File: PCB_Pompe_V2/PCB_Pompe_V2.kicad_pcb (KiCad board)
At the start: 4 copper layers, 89.8 x 59.2 mm, 197 parts, among them J1 Conn_01x04_Female, J10 Conn_01x03_Female, J11 Conn_01x03_Female, J12 Conn_01x03_Female, J13 Conn_01x05_Female, J14 Conn_01x03_Female, J15 Conn_01x03_Female, J16 Conn_01x03_Female, J17 Conn_01x03_Female, J18 Conn_01x03_Female, J19 Conn_01x03_Female, J2 Conn_01x04_Female, J3 Conn_01x03_Female, J4 Conn_01x03_Female, J5 Conn_01x03_Female, J6 Conn_01x03_Female, J7 Conn_01x03_Female, J8 Conn_01x02_Male, J9 Conn_01x03_Female, Q1 DMN10H700S, Q10 DMN10H700S, Q11 DMN10H700S, Q12 DMN10H700S, Q13 DMN10H700S, Q14 DMN10H700S, Q15 DMN10H700S, Q16 DMN10H700S, Q17 DMN10H700S, Q18 DMN10H700S, Q19 DMN10H700S, Q2 DMN10H700S, Q20 DMN10H700S, Q21 DMN10H700S, Q22 DMN10H700S, Q23 DMN10H700S, Q24 DMN10H700S, Q25 DMN10H700S, Q26 DMN10H700S, Q27 DMN10H700S, Q28 DMN10H700S, Q29 DMN10H700S, Q3 DMN10H700S, Q30 DMN10H700S, Q4 DMN10H700S, Q5 DMN10H700S, Q6 DMN10H700S, Q7 DMN10H700S, Q8 DMN10H700S, Q9 DMN10H700S, U1 SN65HVD232, U2 STM32F302C6Tx, U3 NCP1117-3.3_SOT223, Y1 8MHz

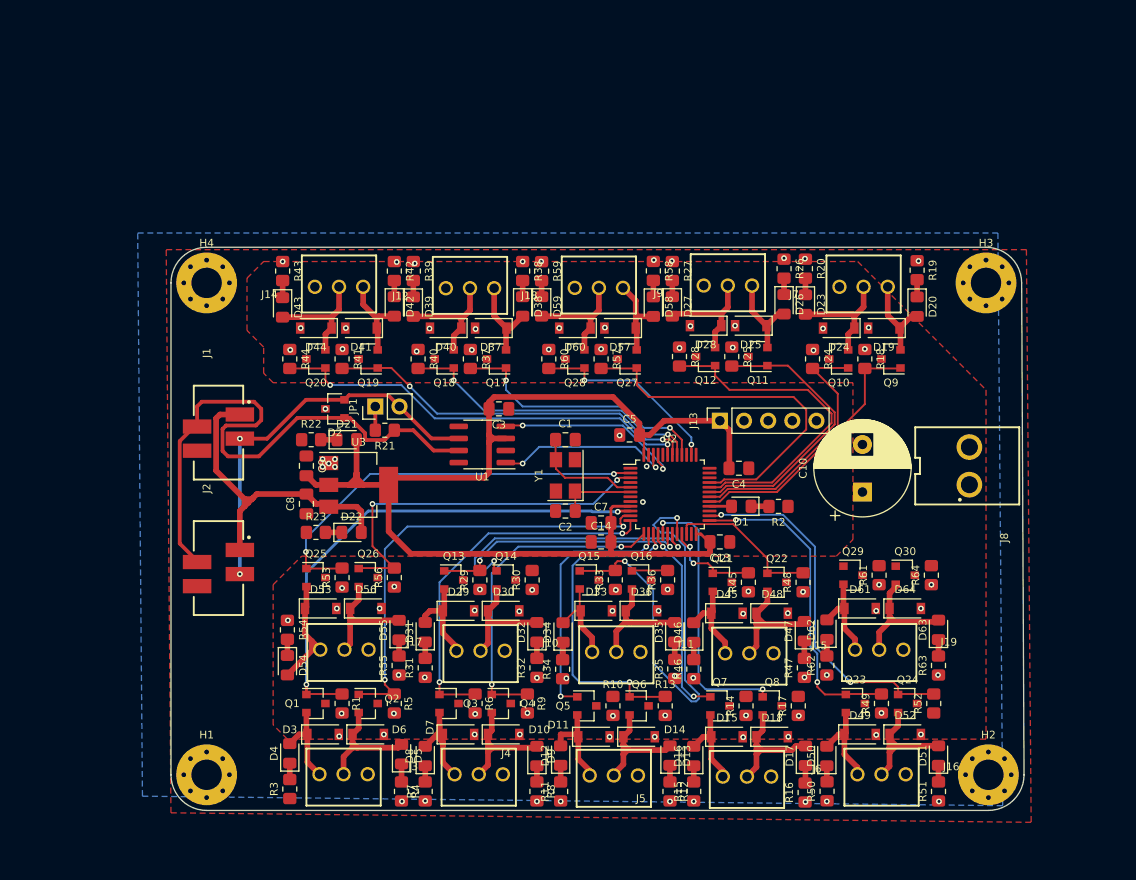
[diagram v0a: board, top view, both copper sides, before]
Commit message: IO prete, Pompe finir sérigraphie, Alim+AX12 à faire
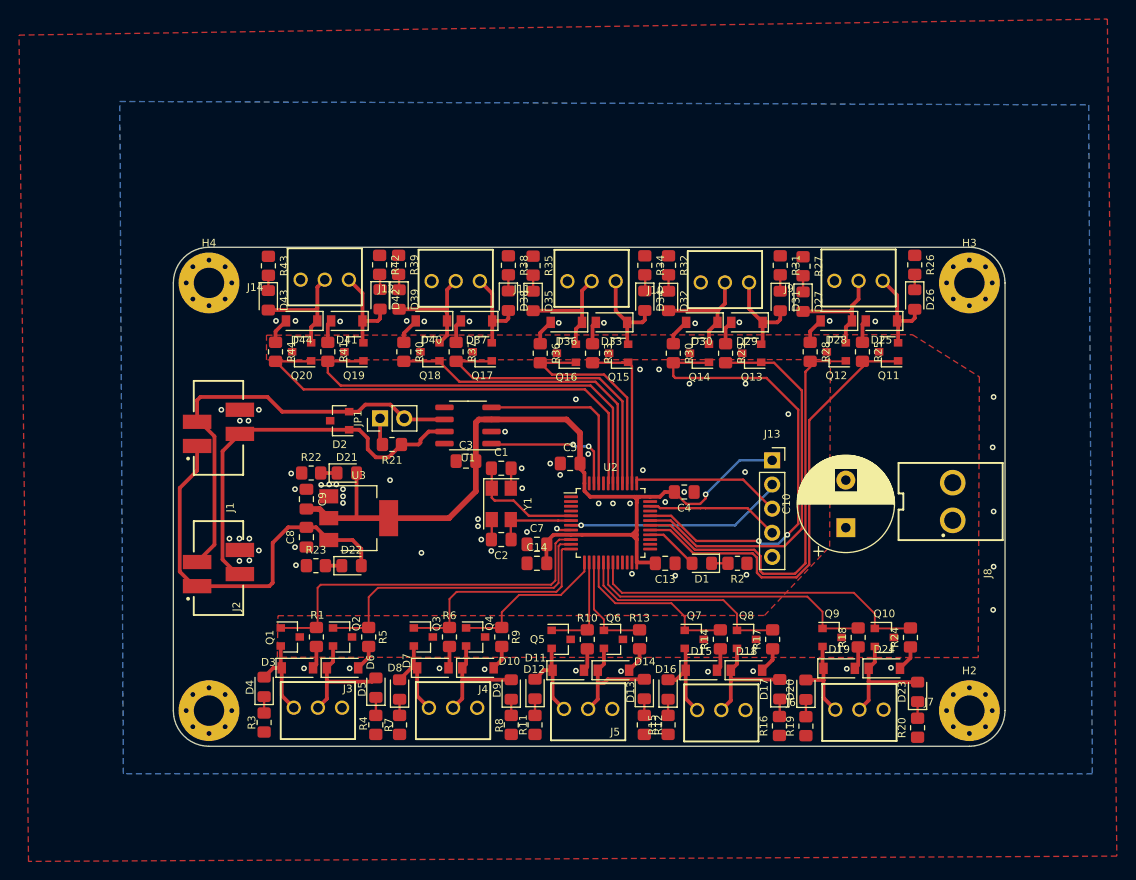
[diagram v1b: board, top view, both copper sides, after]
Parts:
- removed D45, D48, D49, D52, D53, D56, D57, D60, D61, D64: D, Diode_SMD:D_SOD-123
- removed D46, D47, D50, D51, D54, D55, D58, D59, D62, D63: LED_DEBUG, LED_SMD:LED_0805_2012Metric_Pad1.15x1.40mm_HandSolder
- removed J15, J16, J17, J18, J19: Conn_01x03_Female, AREA_lib_Connector:Wuerth_2.54mm_3pins_61900311121
- removed Q21, Q22, Q23, Q24, Q25, Q26, Q27, Q28, Q29, Q30: DMN10H700S, Package_TO_SOT_SMD:SOT-23
- removed R45, R48, R49, R52, R53, R56, R57, R60, R61, R64: 10k, Resistor_SMD:R_0805_2012Metric_Pad1.20x1.40mm_HandSolder
- removed R46, R47, R50, R51, R54, R55, R58, R59, R62, R63: 560, Resistor_SMD:R_0805_2012Metric_Pad1.20x1.40mm_HandSolder
- moved R31 56.5 mm to (164.8, 76.2), turned to 270 degrees
- moved D31 51.1 mm to (164.8, 79.9), turned to 270 degrees
- moved R20 49.7 mm to (179.3, 124.8), turned to 90 degrees
- moved R19 49.4 mm to (167.6, 124.6), turned to 90 degrees
- moved J10 47.0 mm to (159.0, 77.6), turned to 180 degrees
- moved J7 45.1 mm to (173.2, 123.2), turned to 0 degrees
- moved R35 45.0 mm to (138.8, 76.2), turned to 270 degrees
- moved R32 44.6 mm to (153.1, 76.2), turned to 270 degrees
- moved R34 43.4 mm to (150.6, 76.2), turned to 270 degrees
- moved D29 42.9 mm to (161.3, 82.2), turned to 180 degrees
- moved D23 42.4 mm to (179.3, 121.0), turned to 90 degrees
- moved D20 42.0 mm to (167.6, 120.8), turned to 90 degrees
- moved J11 39.7 mm to (145.0, 77.5), turned to 180 degrees
- moved Q13 39.4 mm to (161.8, 85.4), turned to 180 degrees
- moved D35 37.9 mm to (138.8, 79.9), turned to 270 degrees
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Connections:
- U1 pad 5: Net-(U1-Pad5) -> (no net)
- U1 pad 8: Net-(U1-Pad8) -> (no net)
- U2 pad 1: Net-(U2-Pad1) -> (no net)
- U2 pad 18: P7 -> P5
- U2 pad 19: V7 -> V5
- U2 pad 2: P13 -> (no net)
- U2 pad 20: P8 -> (no net)
- U2 pad 21: P11 -> (no net)
- U2 pad 22: V11 -> (no net)
- U2 pad 25: P12 -> (no net)
- U2 pad 26: V12 -> (no net)
- U2 pad 27: P15 -> (no net)
- U2 pad 29: P5 -> P6
- U2 pad 3: V13 -> (no net)
- U2 pad 30: V5 -> V6
- U2 pad 31: P6 -> P7
- U2 pad 32: V6 -> V7
- U2 pad 33: P14 -> (no net)
- U2 pad 38: V14 -> P8
- U2 pad 4: V15 -> (no net)
- U2 pad 44: /BOOT -> (no net)
- Y1 pad 1: Net-(C2-Pad1) -> Net-(C1-Pad1)
- Y1 pad 3: Net-(C1-Pad1) -> Net-(C2-Pad1)
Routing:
- net GND: track 0.33 -> 56.9 mm, vias 97 -> 77
- net P13: track 44.0 -> 0.00 mm, vias 2 -> 0
- net V13: track 39.7 -> 0.00 mm, vias 2 -> 0
- net P14: track 39.0 -> 0.00 mm
- net V12: track 38.1 -> 0.00 mm, vias 2 -> 0
- net P12: track 33.8 -> 0.00 mm, vias 2 -> 0
- net P8: track 49.5 -> 17.4 mm, vias 2 -> 0
- net +3V3: track 125.4 -> 95.4 mm, vias 0 -> 1
- net RST: track 0.00 -> 23.2 mm, vias 0 -> 1
- net V3: track 34.1 -> 11.3 mm, vias 2 -> 0
- net CANH: track 62.7 -> 41.3 mm
- net V14: track 20.6 -> 0.00 mm, vias 2 -> 0
- net V7: track 29.4 -> 49.5 mm
- net V8: track 3.77 -> 23.5 mm
- net P6: track 30.3 -> 47.8 mm
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- removed copper zone on In1.Cu, net +5VP
- removed copper zone on In2.Cu, net GND
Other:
- board size 89.8 x 59.2 mm -> 87.5 x 52.5 mm
- copper layers 4 -> 2
